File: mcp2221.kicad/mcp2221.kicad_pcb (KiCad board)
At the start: 2 copper layers, 47.2 x 34.6 mm, 25 parts, among them J1 Jumper 32 or 21, J2 Conn_01x04_Male, J3 Conn_01x03_Male, J4 Conn_01x06_Male, J5 Conn_01x03_Male, J6 Conn_01x06_Male, J7 Conn_01x02_Male, J8 Conn_01x02_Male, SW1 SW_Push, U1 AMS1117CD-3.3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

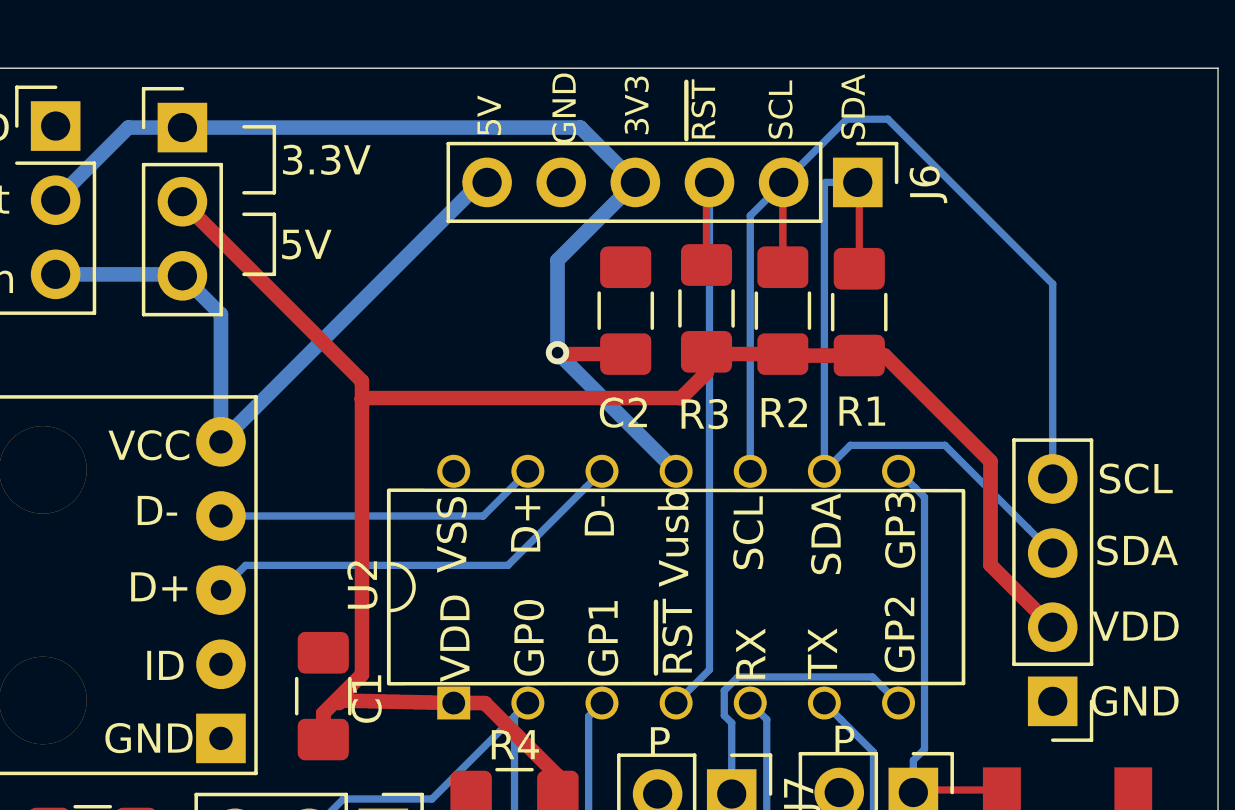
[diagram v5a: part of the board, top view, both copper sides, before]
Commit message: moved C2 and R1-R3 to MCP2221
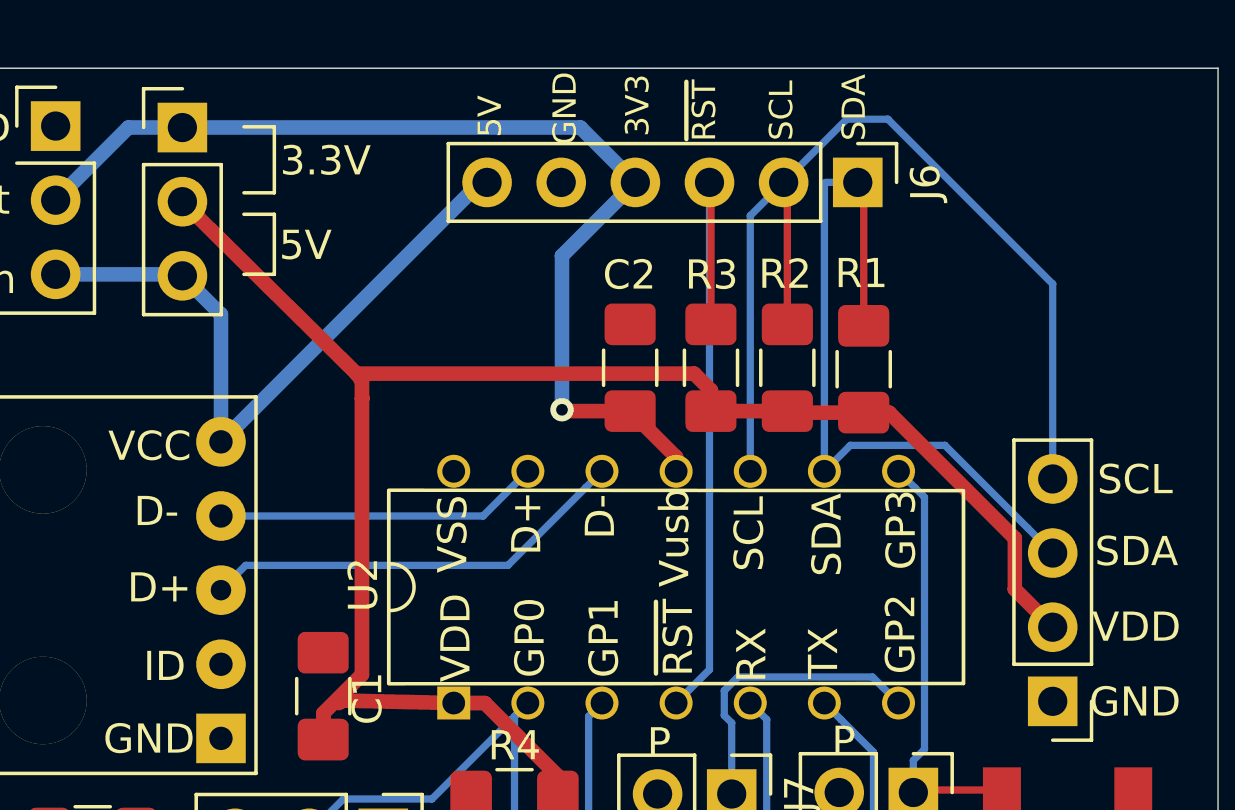
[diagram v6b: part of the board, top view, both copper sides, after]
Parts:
- moved R3 2.04 mm to (94.2, 57.3)
- moved C2 1.96 mm to (91.4, 57.3)
- moved R2 1.96 mm to (96.8, 57.3)
- moved R1 1.96 mm to (99.4, 57.4)
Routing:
- net /~RST~: track 21.2 -> 23.3 mm
- net /SDA: track 23.7 -> 25.8 mm
- net /SCL: track 32.4 -> 34.5 mm
- net /VDD: track 77.1 -> 75.2 mm
- net /3.3V: track 36.7 -> 35.5 mm
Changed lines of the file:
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@@
     (thickness 1.6)
     (drawings 35)
-    (tracks 133)
+    (tracks 136)
     (zones 0)
     (modules 25)
@@
   )
   (module Resistor_SMD:R_1206_3216Metric_Pad1.42x1.75mm_HandSolder (layer F.Cu)
-    (at 94.0054 55.2958 270)
+    (at 94.1578 57.3278 270)
     (descr "Resistor SMD 1206 (3216 Metric), square (rectangular) end terminal, IPC_7351 nominal with elongated pad for handsoldering. (Body size source: http://www.tortai-tech.com/upload/download/2011102023233369053.pdf), generated with kicad-footprint-generator")
     (tags "resistor handsolder")
     (attr smd)
-    (fp_text reference R3 (at 3.6576 0.0762 180) (layer F.SilkS)
+    (fp_text reference R3 (at -3.175 -0.0254 180) (layer F.SilkS)
       (effects (font (size 1 1) (thickness 0.15)))
     )
@@
   )
   (module Resistor_SMD:R_1206_3216Metric_Pad1.42x1.75mm_HandSolder (layer F.Cu)
-    (at 96.6216 55.372 90)
+    (at 96.774 57.3278 90)
     (descr "Resistor SMD 1206 (3216 Metric), square (rectangular) end terminal, IPC_7351 nominal with elongated pad for handsoldering. (Body size source: http://www.tortai-tech.com/upload/download/2011102023233369053.pdf), generated with kicad-footprint-generator")
     (tags "resistor handsolder")
     (attr smd)
-    (fp_text reference R2 (at -3.5306 0.0508 180) (layer F.SilkS)
+    (fp_text reference R2 (at 3.2004 -0.0762 180) (layer F.SilkS)
       (effects (font (size 1 1) (thickness 0.15)))
     )
@@
   )
   (module Resistor_SMD:R_1206_3216Metric_Pad1.42x1.75mm_HandSolder (layer F.Cu)
-    (at 99.2378 55.4228 90)
+    (at 99.3902 57.3786 90)
     (descr "Resistor SMD 1206 (3216 Metric), square (rectangular) end terminal, IPC_7351 nominal with elongated pad for handsoldering. (Body size source: http://www.tortai-tech.com/upload/download/2011102023233369053.pdf), generated with kicad-footprint-generator")
     (tags "resistor handsolder")
     (attr smd)
-    (fp_text reference R1 (at -3.429 0.1016 180) (layer F.SilkS)
+    (fp_text reference R1 (at 3.2766 -0.0762 180) (layer F.SilkS)
       (effects (font (size 1 1) (thickness 0.15)))
     )
@@
   )
   (module Capacitor_SMD:C_1206_3216Metric_Pad1.42x1.75mm_HandSolder (layer F.Cu)
-    (at 91.2368 55.372 90)
+    (at 91.3892 57.3278 90)
     (descr "Capacitor SMD 1206 (3216 Metric), square (rectangular) end terminal, IPC_7351 nominal with elongated pad for handsoldering. (Body size source: http://www.tortai-tech.com/upload/download/2011102023233369053.pdf), generated with kicad-footprint-generator")
     (tags "capacitor handsolder")
     (attr smd)
-    (fp_text reference C2 (at -3.5306 -0.0508 180) (layer F.SilkS)
+    (fp_text reference C2 (at 3.175 -0.0254 180) (layer F.SilkS)
       (effects (font (size 1 1) (thickness 0.15)))
     )
@@
   (segment (start 89.0159 74.7522) (end 89.0159 72.1106) (width 0.5) (layer F.Cu) (net 2))
   (segment (start 80.8736 69.355) (end 80.8736 70.0675) (width 0.5) (layer F.Cu) (net 2))
-  (segment (start 96.6724 56.9103) (end 96.6216 56.8595) (width 0.5) (layer F.Cu) (net 2))
-  (segment (start 99.2378 56.9103) (end 96.6724 56.9103) (width 0.5) (layer F.Cu) (net 2))
   (segment (start 85.344 68.8162) (end 81.5594 68.7324) (width 0.5) (layer F.Cu) (net 2))
   (segment (start 81.5594 68.7324) (end 81.4124 68.8162) (width 0.5) (layer F.Cu) (net 2))
-  (segment (start 94.0816 56.8595) (end 94.0054 56.7833) (width 0.5) (layer F.Cu) (net 2))
-  (segment (start 96.6216 56.8595) (end 94.0816 56.8595) (width 0.5) (layer F.Cu) (net 2))
-  (segment (start 94.0054 57.4958) (end 93.132 58.3692) (width 0.5) (layer F.Cu) (net 2))
-  (segment (start 93.132 58.3692) (end 82.2198 58.3692) (width 0.5) (layer F.Cu) (net 2))
-  (segment (start 94.0054 56.7833) (end 94.0054 57.4958) (width 0.5) (layer F.Cu) (net 2))
   (segment (start 82.19861 58.39039) (end 82.2198 58.3692) (width 0.5) (layer F.Cu) (net 2))
   (segment (start 86.409 68.8162) (end 88.9143 71.3215) (width 0.5) (layer F.Cu) (net 2))
@@
   (segment (start 98.8171 75.9066) (end 98.8171 75.0316) (width 0.5) (layer F.Cu) (net 2))
   (segment (start 91.5781 75.0316) (end 91.5781 75.9066) (width 0.5) (layer F.Cu) (net 2))
-  (segment (start 100.1128 56.9103) (end 103.7336 60.5311) (width 0.5) (layer F.Cu) (net 2))
-  (segment (start 99.2378 56.9103) (end 100.1128 56.9103) (width 0.5) (layer F.Cu) (net 2))
-  (segment (start 103.7336 64.0842) (end 105.8672 66.2178) (width 0.5) (layer F.Cu) (net 2))
-  (segment (start 103.7336 60.5311) (end 103.7336 64.0842) (width 0.5) (layer F.Cu) (net 2))
   (segment (start 80.8736 69.169966) (end 82.19861 67.844956) (width 0.5) (layer F.Cu) (net 2))
   (segment (start 82.19861 67.844956) (end 82.19861 58.39039) (width 0.5) (layer F.Cu) (net 2))
   (segment (start 80.8736 70.0675) (end 80.8736 69.169966) (width 0.5) (layer F.Cu) (net 2))
-  (segment (start 82.19861 57.78921) (end 76.0476 51.6382) (width 0.5) (layer F.Cu) (net 2))
   (segment (start 82.19861 58.39039) (end 82.19861 57.78921) (width 0.5) (layer F.Cu) (net 2))
+  (segment (start 96.8248 58.8661) (end 96.774 58.8153) (width 0.5) (layer F.Cu) (net 2))
+  (segment (start 99.3902 58.8661) (end 96.8248 58.8661) (width 0.5) (layer F.Cu) (net 2))
+  (segment (start 96.774 58.8153) (end 94.1578 58.8153) (width 0.5) (layer F.Cu) (net 2))
+  (segment (start 100.2652 58.8661) (end 99.3902 58.8661) (width 0.5) (layer F.Cu) (net 2))
+  (segment (start 104.567199 63.168099) (end 100.2652 58.8661) (width 0.5) (layer F.Cu) (net 2))
+  (segment (start 104.567199 64.917799) (end 104.567199 63.168099) (width 0.5) (layer F.Cu) (net 2))
+  (segment (start 105.8672 66.2178) (end 104.567199 64.917799) (width 0.5) (layer F.Cu) (net 2))
+  (segment (start 94.1578 58.1028) (end 93.586 57.531) (width 0.5) (layer F.Cu) (net 2))
+  (segment (start 94.1578 58.8153) (end 94.1578 58.1028) (width 0.5) (layer F.Cu) (net 2))
+  (segment (start 82.19861 57.78921) (end 82.0166 57.531) (width 0.5) (layer F.Cu) (net 2))
+  (segment (start 93.586 57.531) (end 82.0166 57.531) (width 0.5) (layer F.Cu) (net 2))
+  (segment (start 82.0166 57.531) (end 76.0476 51.6382) (width 0.5) (layer F.Cu) (net 2))
   (segment (start 68.9499 73.279) (end 68.8991 73.2282) (width 0.25) (layer F.Cu) (net 3))
   (segment (start 71.4867 73.279) (end 68.9499 73.279) (width 0.25) (layer F.Cu) (net 3))
@@
   (segment (start 92.964 68.8162) (end 94.107 67.6732) (width 0.25) (layer B.Cu) (net 5))
   (segment (start 94.0054 51.0794) (end 94.107 50.9778) (width 0.25) (layer F.Cu) (net 5))
-  (segment (start 94.0054 53.8083) (end 94.0054 51.0794) (width 0.25) (layer F.Cu) (net 5))
+  (segment (start 94.1578 51.0286) (end 94.107 50.9778) (width 0.25) (layer F.Cu) (net 5))
+  (segment (start 94.1578 55.8403) (end 94.1578 51.0286) (width 0.25) (layer F.Cu) (net 5))
   (segment (start 98.608999 69.381199) (end 98.044 68.8162) (width 0.25) (layer B.Cu) (net 6))
   (segment (start 99.727001 70.499201) (end 98.608999 69.381199) (width 0.25) (layer B.Cu) (net 6))
@@
   (segment (start 105.8672 54.458598) (end 100.220801 48.812199) (width 0.25) (layer B.Cu) (net 12))
   (segment (start 96.6216 51.0032) (end 96.647 50.9778) (width 0.25) (layer F.Cu) (net 12))
-  (segment (start 96.6216 53.8845) (end 96.6216 51.0032) (width 0.25) (layer F.Cu) (net 12))
+  (segment (start 96.774 51.1048) (end 96.647 50.9778) (width 0.25) (layer F.Cu) (net 12))
+  (segment (start 96.774 55.8403) (end 96.774 51.1048) (width 0.25) (layer F.Cu) (net 12))
   (segment (start 105.017201 62.827801) (end 105.8672 63.6778) (width 0.25) (layer B.Cu) (net 13))
   (segment (start 102.175599 59.986199) (end 105.017201 62.827801) (width 0.25) (layer B.Cu) (net 13))
@@
   (segment (start 98.044 60.8762) (end 98.044 51.0208) (width 0.25) (layer B.Cu) (net 13))
   (segment (start 99.2378 51.0286) (end 99.187 50.9778) (width 0.25) (layer F.Cu) (net 13))
-  (segment (start 99.2378 53.9353) (end 99.2378 51.0286) (width 0.25) (layer F.Cu) (net 13))
+  (segment (start 99.3902 51.181) (end 99.187 50.9778) (width 0.25) (layer F.Cu) (net 13))
+  (segment (start 99.3902 55.8911) (end 99.3902 51.181) (width 0.25) (layer F.Cu) (net 13))
   (segment (start 86.3524 62.4078) (end 87.884 60.8762) (width 0.25) (layer B.Cu) (net 14))
   (segment (start 77.3684 62.4078) (end 86.3524 62.4078) (width 0.25) (layer B.Cu) (net 14))
@@
   (segment (start 74.1934 49.0982) (end 76.0476 49.0982) (width 0.5) (layer B.Cu) (net 17))
   (segment (start 71.7042 51.5874) (end 74.1934 49.0982) (width 0.5) (layer B.Cu) (net 17))
-  (segment (start 92.964 60.8762) (end 88.9 56.8122) (width 0.5) (layer B.Cu) (net 17))
-  (via (at 88.9 56.8122) (size 0.8) (drill 0.4) (layers F.Cu B.Cu) (net 17))
-  (segment (start 91.2368 56.8595) (end 88.9473 56.8595) (width 0.5) (layer F.Cu) (net 17))
-  (segment (start 88.9473 56.8595) (end 88.9 56.8122) (width 0.5) (layer F.Cu) (net 17))
-  (segment (start 88.9 53.6448) (end 91.567 50.9778) (width 0.5) (layer B.Cu) (net 17))
-  (segment (start 88.9 56.8122) (end 88.9 53.6448) (width 0.5) (layer B.Cu) (net 17))
+  (via (at 89.0524 58.768) (size 0.8) (drill 0.4) (layers F.Cu B.Cu) (net 17))
+  (segment (start 91.3892 58.8153) (end 89.0997 58.8153) (width 0.5) (layer F.Cu) (net 17))
   (segment (start 89.6874 49.0982) (end 76.0476 49.0982) (width 0.5) (layer B.Cu) (net 17))
   (segment (start 91.567 50.9778) (end 89.6874 49.0982) (width 0.5) (layer B.Cu) (net 17))
+  (segment (start 92.964 60.3901) (end 91.3892 58.8153) (width 0.5) (layer F.Cu) (net 17))
+  (segment (start 92.964 60.8762) (end 92.964 60.3901) (width 0.5) (layer F.Cu) (net 17))
+  (segment (start 89.0524 53.4924) (end 91.567 50.9778) (width 0.5) (layer B.Cu) (net 17))
+  (segment (start 89.0524 58.768) (end 89.0524 53.4924) (width 0.5) (layer B.Cu) (net 17))
   (segment (start 71.7042 54.1274) (end 75.9968 54.1274) (width 0.5) (layer B.Cu) (net 18))
   (segment (start 77.3684 59.8678) (end 86.4108 50.8254) (width 0.5) (layer B.Cu) (net 18))

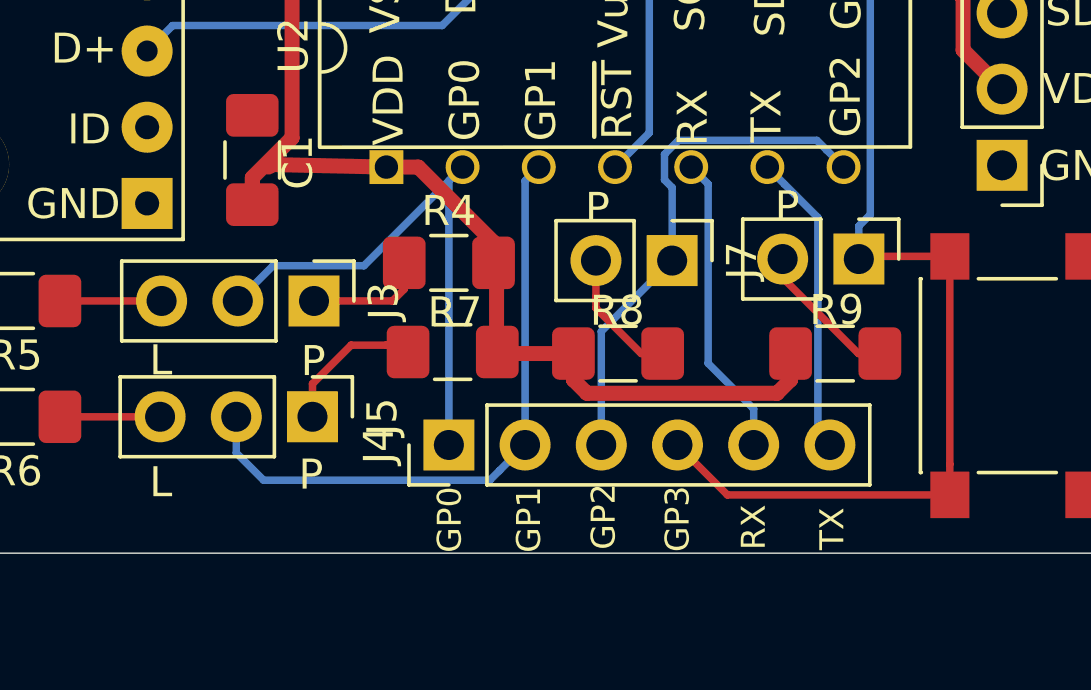
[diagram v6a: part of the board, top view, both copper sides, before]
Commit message: added labels
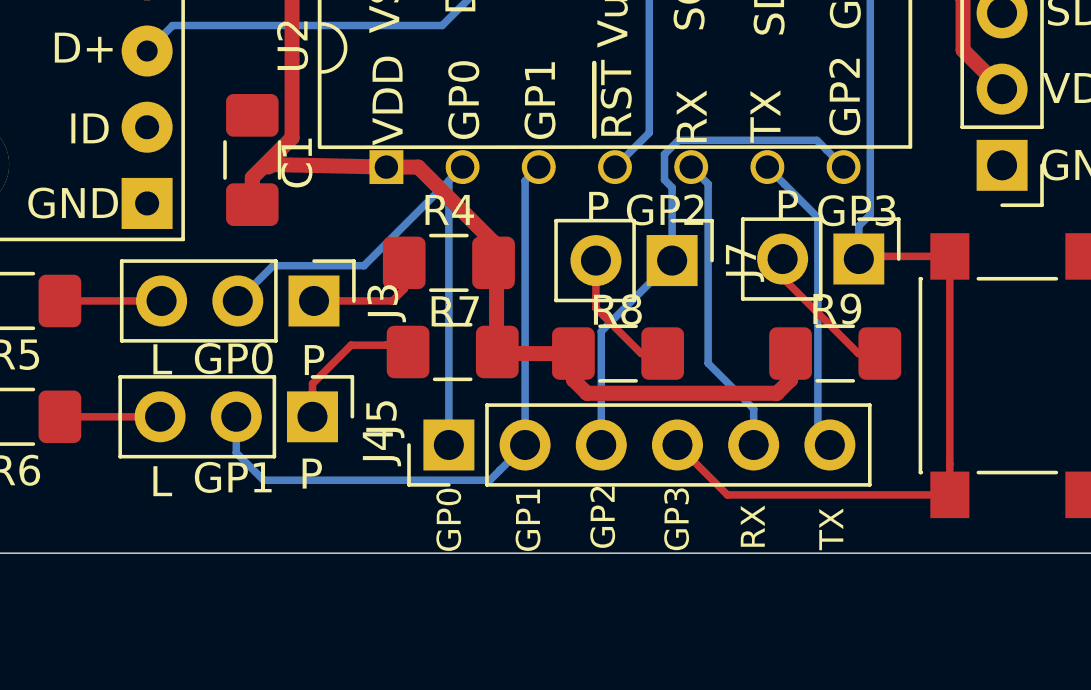
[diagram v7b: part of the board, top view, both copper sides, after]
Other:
- board text added: "Rev 6"
- board text added: "https://github.com/bablokb/pcb-mcp2221"
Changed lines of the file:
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@@
   (general
     (thickness 1.6)
-    (drawings 35)
+    (drawings 41)
     (tracks 136)
     (zones 0)
@@
       (net 1 GND))
   )
+  (gr_text GP3 (at 101.0412 70.3072) (layer F.SilkS)
+    (effects (font (size 1 1) (thickness 0.15)))
+  )
+  (gr_text GP2 (at 94.6658 70.2818) (layer F.SilkS)
+    (effects (font (size 1 1) (thickness 0.15)))
+  )
+  (gr_text GP1 (at 80.264 79.1972) (layer F.SilkS)
+    (effects (font (size 1 1) (thickness 0.15)))
+  )
+  (gr_text GP0 (at 80.264 75.2348) (layer F.SilkS)
+    (effects (font (size 1 1) (thickness 0.15)))
+  )
+  (gr_text "Rev 6" (at 67.7926 80.2894) (layer B.SilkS)
+    (effects (font (size 1 1) (thickness 0.15)) (justify mirror))
+  )
+  (gr_text https://github.com/bablokb/pcb-mcp2221 (at 94.361 80.3148) (layer B.SilkS)
+    (effects (font (size 1 1) (thickness 0.15)) (justify mirror))
+  )
   (gr_text 3.3V (at 80.9498 50.2412) (layer F.SilkS)
